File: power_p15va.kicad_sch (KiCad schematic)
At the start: 29 parts, among them U8 LT8350S, U9 LT3042

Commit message: edit README.md
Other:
- company: (none) -> NOIRLab
- title: (none) -> 4 channel ADC Module
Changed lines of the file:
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@@
 	(generator_version "9.0")
 	(paper "A4")
+	(title_block
+		(title "4 channel ADC Module")
+		(date "2025-04-18")
+		(rev "0.1")
+		(company "NOIRLab")
+		(comment 1 "Design: Braulio Cancino Vera - braulio.cancino@noirlab.edu")
+	)
 	(text "OUTS and SET GND kelvin \nconnected to output capacitor\nto improve PSRR"
 		(exclude_from_sim no)

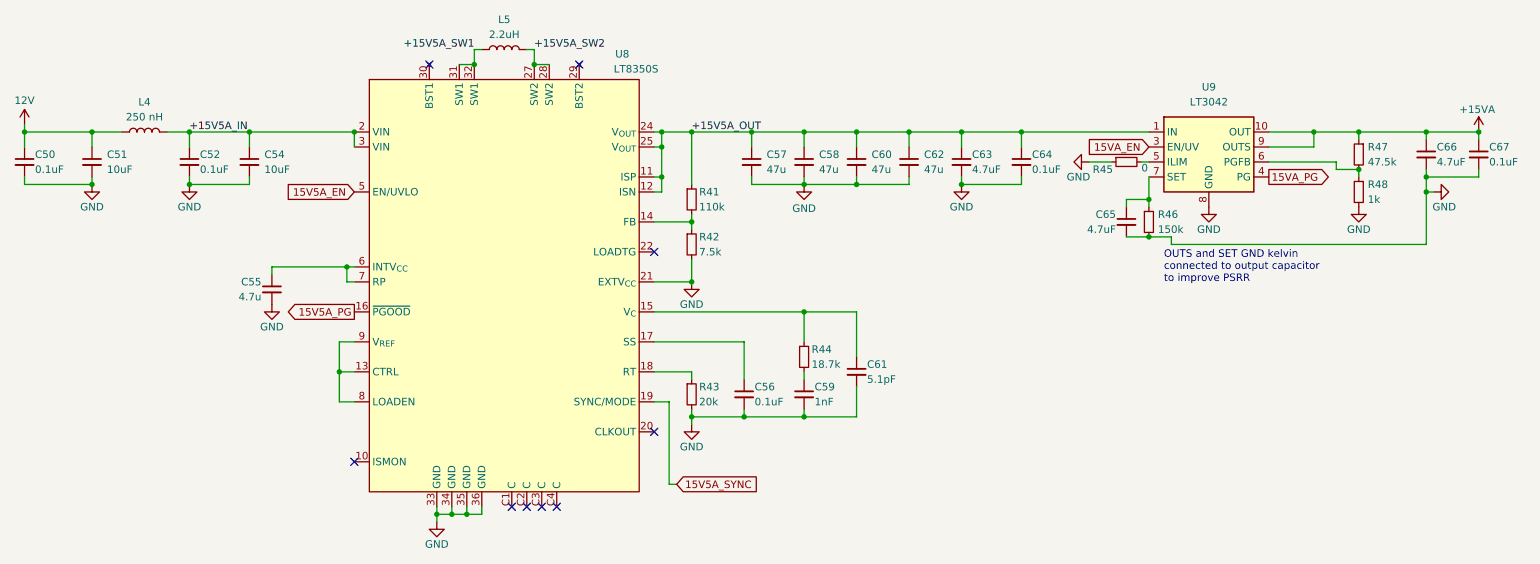
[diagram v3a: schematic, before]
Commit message: Split DC DC schematic and improve layout
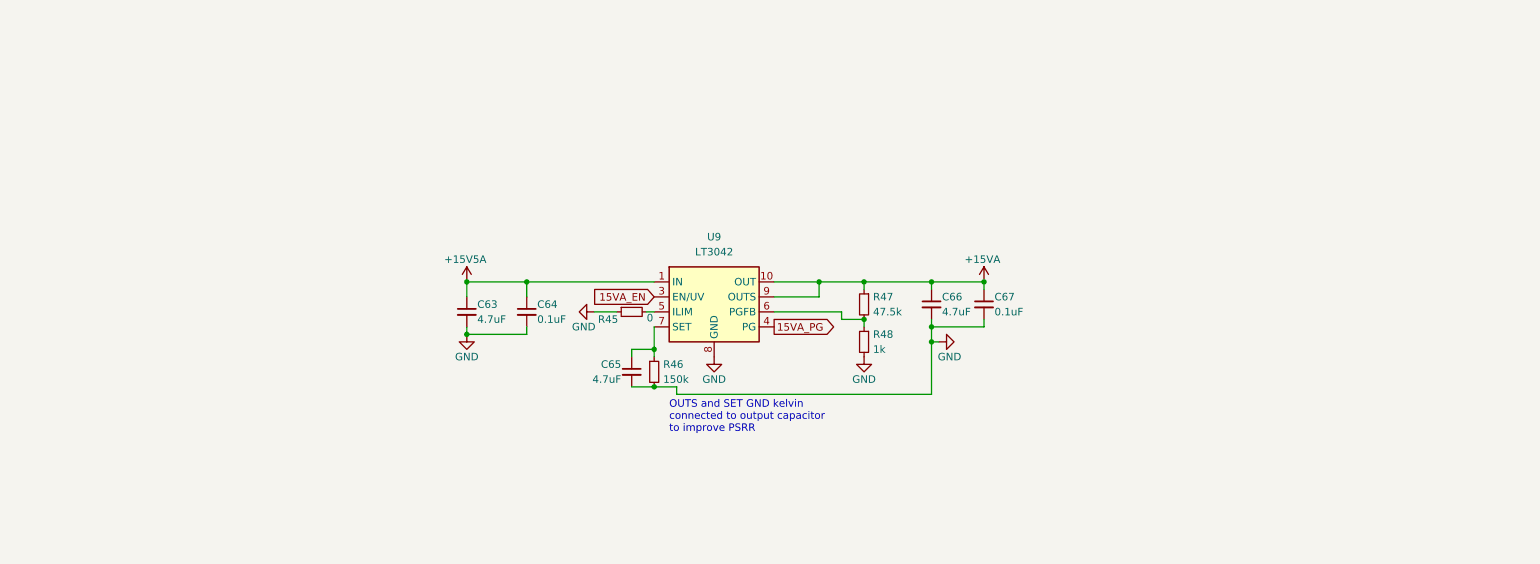
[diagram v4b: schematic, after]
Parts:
- removed C50, C52, C56: 0.1uF, Capacitor_SMD:C_0402_1005Metric, symbol Device:C_Small
- removed C51, C54: 10uF, Capacitor_SMD:C_1206_3216Metric, symbol Device:C_Small
- removed C55: 4.7u, Capacitor_SMD:C_0603_1608Metric, symbol Device:C_Small
- removed C57, C58, C60, C62: 47u, Capacitor_SMD:C_1210_3225Metric, symbol Device:C_Small
- removed C59: 1nF, Capacitor_SMD:C_0603_1608Metric, symbol Device:C_Small
- removed C61: 5.1pF, Capacitor_SMD:C_0603_1608Metric, symbol Device:C_Small
- removed L4: 250 nH, Inductor_SMD:L_1210_3225Metric, symbol Device:L
- removed L5: 2.2uH, lib:XGL1313, symbol Device:L
- removed R41: 110k, Resistor_SMD:R_0603_1608Metric, symbol Device:R_Small
- removed R42: 7.5k, Resistor_SMD:R_0603_1608Metric, symbol Device:R_Small
- removed R43: 20k, Resistor_SMD:R_0603_1608Metric, symbol Device:R_Small
- removed R44: 18.7k, Resistor_SMD:R_0603_1608Metric, symbol Device:R_Small
- removed U8: LT8350S, lib:LT8350S, symbol lib:LT8350S
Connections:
- net +15V5A_OUT renamed +15V5A
- no-connect marks 9 -> 0
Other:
- moved on the sheet: C63, C64, C65, C66, C67, R45, R46, R47, R48, U9
